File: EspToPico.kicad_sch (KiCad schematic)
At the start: 13 parts, among them J1 Conn_01x20_Pin, J2 Conn_01x20_Pin, J3 USB_C_Receptacle_USB2.0_16P, U2 AP2112K-3.3, U3 TPD3E001DRLR, U4 ESP32-S3-WROOM-1

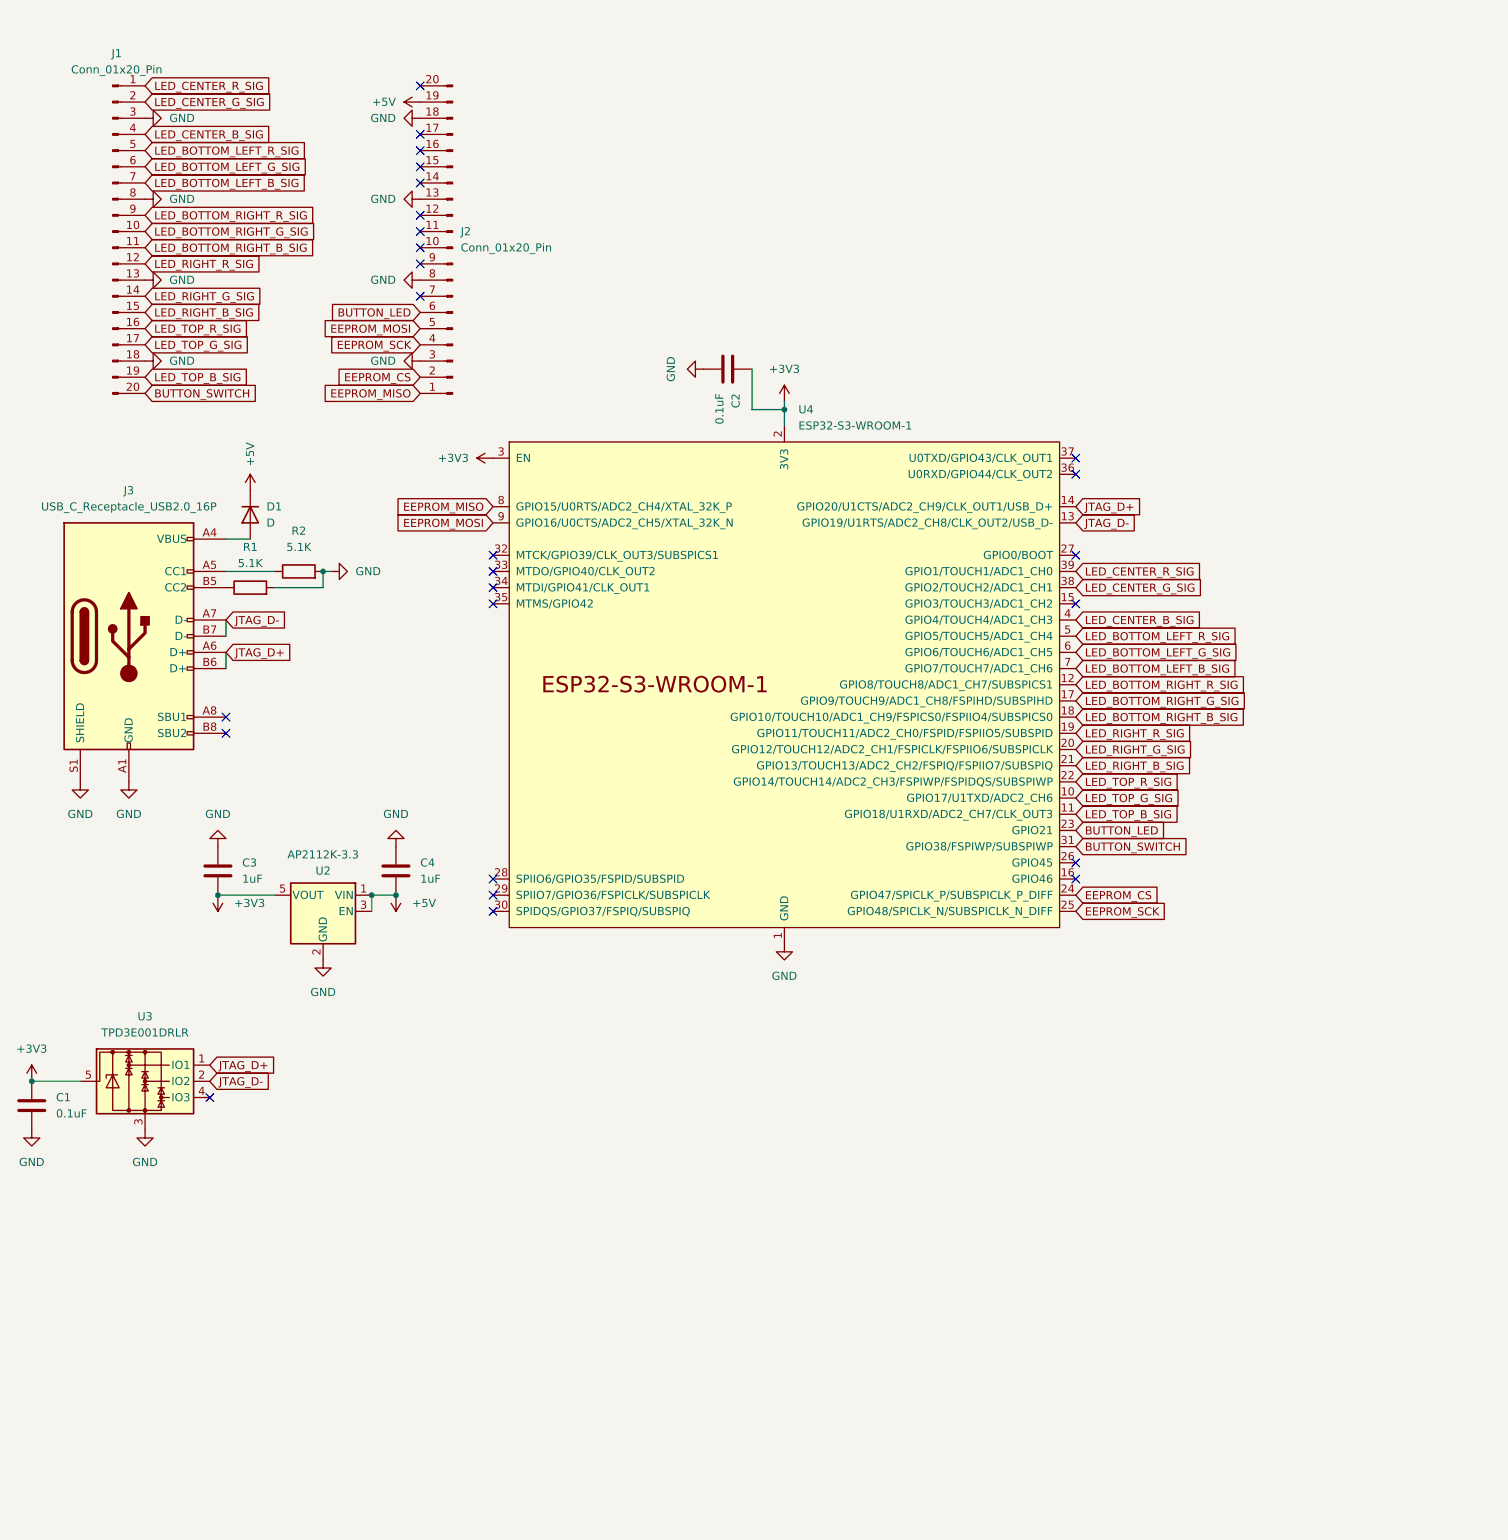
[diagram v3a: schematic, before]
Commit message: Started conversion to ESP32
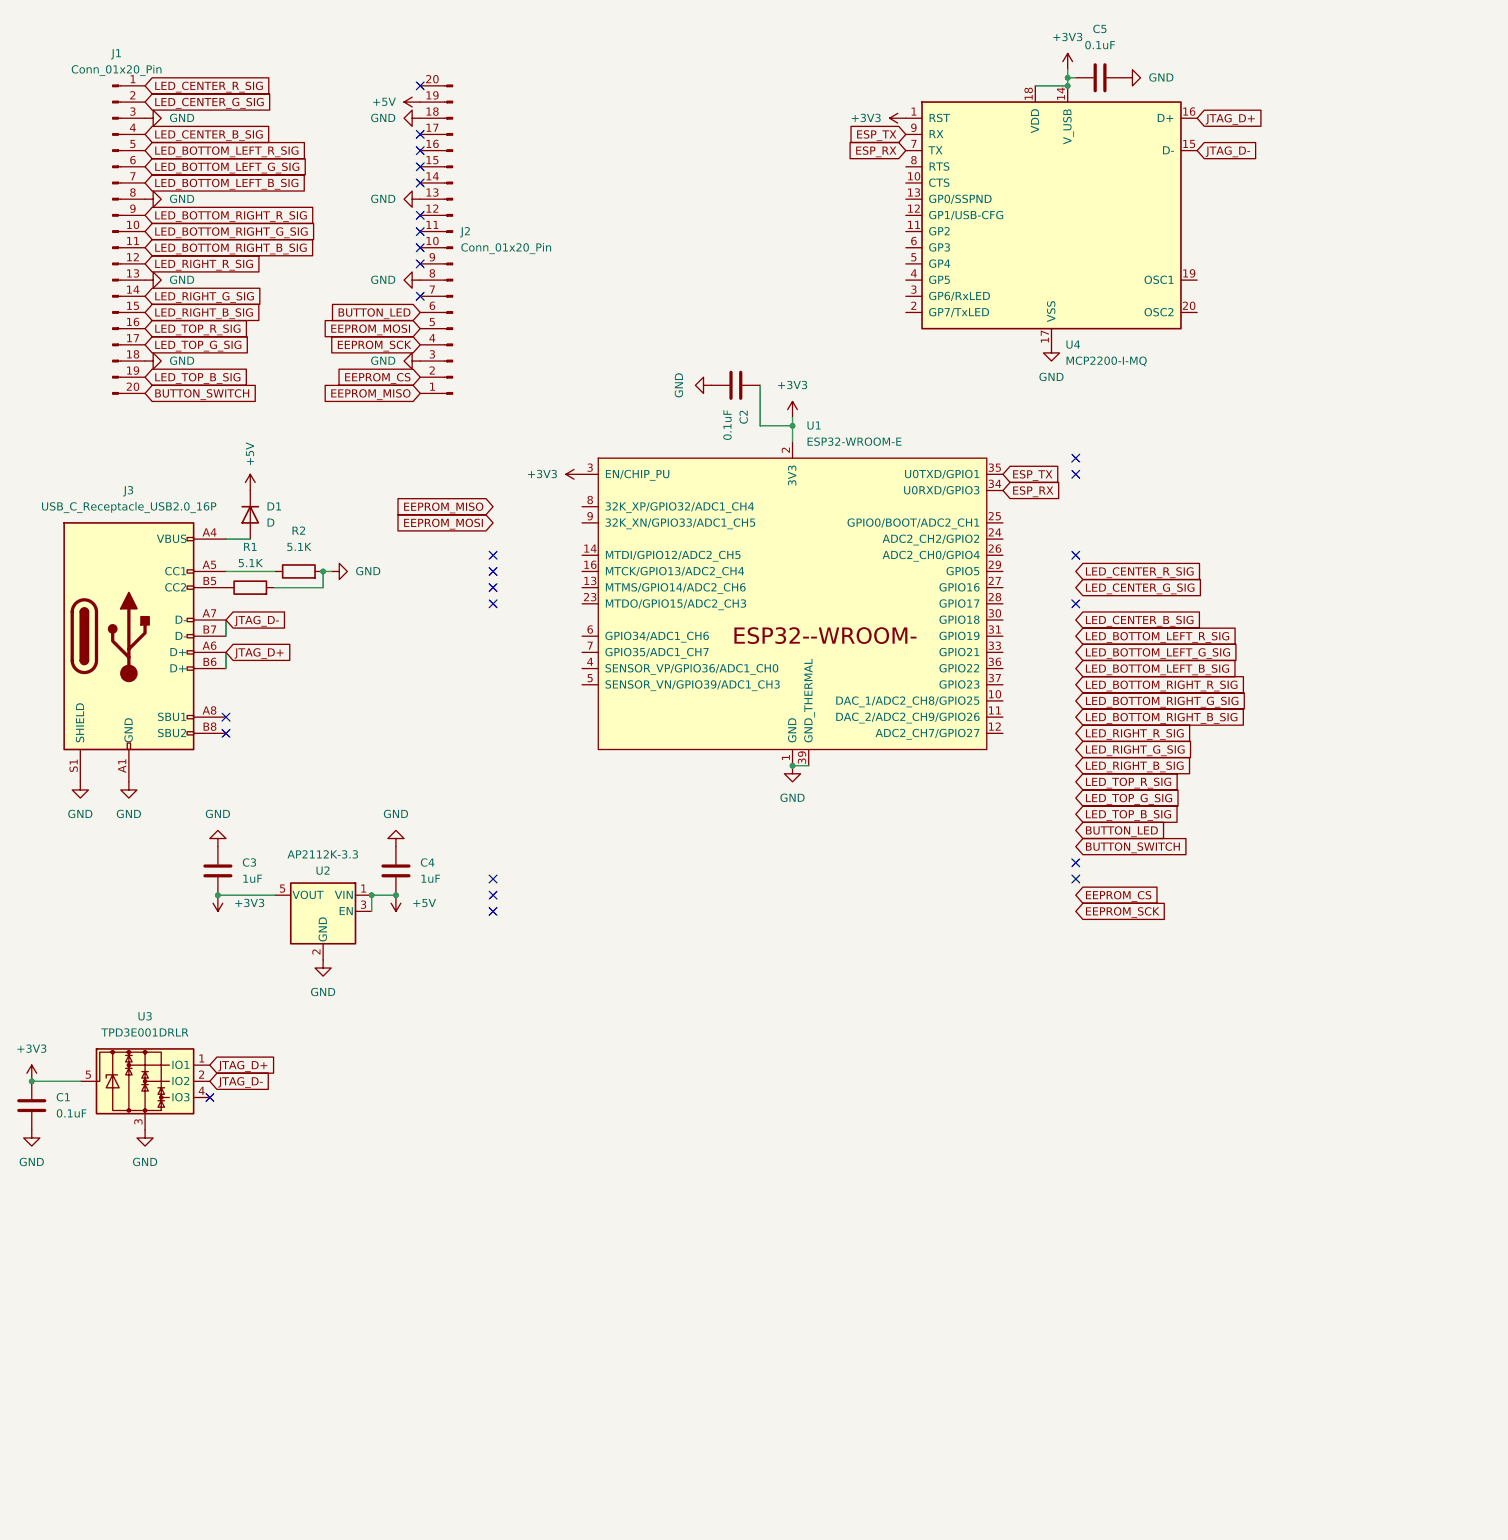
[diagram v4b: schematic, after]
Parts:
- removed U4: ESP32-S3-WROOM-1, PCM_Espressif:ESP32-S3-WROOM-1, symbol PCM_Espressif:ESP32-S3-WROOM-1
- added C5: 0.1uF, symbol Device:C
- added U1: ESP32-WROOM-E, PCM_Espressif:ESP32-WROOM-32E, symbol PCM_Espressif:ESP32-WROOM-E
- added U4: MCP2200-I-MQ, Package_DFN_QFN:QFN-20-1EP_5x5mm_P0.65mm_EP3.35x3.35mm, symbol Interface_USB:MCP2200-I-MQ
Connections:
- net +3V3: now also C5.1, U1.2 (3V3), U1.3 (EN/CHIP_PU), U4.1 (RST), U4.14 (V_USB), U4.18 (VDD)
- net GND: now also C5.2, U1.1 (GND), U1.15 (GND), U1.38 (GND), U1.39 (GND_THERMAL), U4.17 (VSS)
- net JTAG_D+: now also U4.16 (D+)
- net JTAG_D-: now also U4.15 (D-)
- new net ESP_RX: U1.34 (U0RXD/GPIO3), U4.7 (TX)
- new net ESP_TX: U1.35 (U0TXD/GPIO1), U4.9 (RX)
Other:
- moved on the sheet: C2

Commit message: Updated to ESP32
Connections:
- net BUTTON_LED: now also U1.4 (SENSOR_VP/GPIO36/ADC1_CH0)
- net BUTTON_SWITCH: now also U1.23 (MTDO/GPIO15/ADC2_CH3)
- net EEPROM_CS: now also U1.7 (GPIO35/ADC1_CH7)
- net EEPROM_MISO: now also U1.8 (32K_XP/GPIO32/ADC1_CH4)
- net EEPROM_MOSI: now also U1.5 (SENSOR_VN/GPIO39/ADC1_CH3)
- net EEPROM_SCK: now also U1.6 (GPIO34/ADC1_CH6)
- net LED_BOTTOM_LEFT_B_SIG: now also U1.29 (GPIO5)
- net LED_BOTTOM_LEFT_G_SIG: now also U1.30 (GPIO18)
- net LED_BOTTOM_LEFT_R_SIG: now also U1.31 (GPIO19)
- net LED_BOTTOM_RIGHT_B_SIG: now also U1.26 (ADC2_CH0/GPIO4)
- net LED_BOTTOM_RIGHT_G_SIG: now also U1.27 (GPIO16)
- net LED_BOTTOM_RIGHT_R_SIG: now also U1.28 (GPIO17)
- net LED_CENTER_B_SIG: now also U1.33 (GPIO21)
- net LED_CENTER_G_SIG: now also U1.36 (GPIO22)
- net LED_CENTER_R_SIG: now also U1.37 (GPIO23)
- net LED_RIGHT_B_SIG: now also U1.11 (DAC_2/ADC2_CH9/GPIO26)
- net LED_RIGHT_G_SIG: now also U1.10 (DAC_1/ADC2_CH8/GPIO25)
- net LED_RIGHT_R_SIG: now also U1.9 (32K_XN/GPIO33/ADC1_CH5)
- net LED_TOP_B_SIG: now also U1.12 (ADC2_CH7/GPIO27)
- net LED_TOP_G_SIG: now also U1.13 (MTMS/GPIO14/ADC2_CH6)
- net LED_TOP_R_SIG: now also U1.14 (MTDI/GPIO12/ADC2_CH5)
- no-connect marks 26 -> 28

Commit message: Electrical and Routing fixes
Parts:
- added Y1: CSTNE12M0GH5L000R0, footprints:CSTCE12M0G15L, symbol Device:Resonator
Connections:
- net GND: now also Y1.2
- net at U4.19 (OSC1): now also Y1.3
- net at U4.20 (OSC2): now also Y1.1
- no-connect marks 28 -> 26
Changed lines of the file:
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@@
 	)
 	(no_connect
-		(at 231.14 54.61)
-	)
-	(no_connect
 		(at 185.42 46.99)
 	)
@@
 		(at 185.42 54.61)
 	)
-	(no_connect
-		(at 231.14 59.69)
+	(wire
+		(pts
+			(xy 237.49 60.96) (xy 259.08 60.96)
+		)
+		(stroke
+			(width 0)
+			(type default)
+		)
 	)
 	(wire
@@
 	(wire
 		(pts
+			(xy 237.49 59.69) (xy 237.49 60.96)
+		)
+		(stroke
+			(width 0)
+			(type default)
+		)
+	)
+	(wire
+		(pts
 			(xy 78.74 110.49) (xy 78.74 107.95)
 		)
@@
 	(wire
 		(pts
+			(xy 231.14 54.61) (xy 237.49 54.61)
+		)
+		(stroke
+			(width 0)
+			(type default)
+		)
+	)
+	(wire
+		(pts
+			(xy 237.49 53.34) (xy 259.08 53.34)
+		)
+		(stroke
+			(width 0)
+			(type default)
+		)
+	)
+	(wire
+		(pts
 			(xy 86.36 100.33) (xy 78.74 100.33)
 		)
@@
 	(wire
 		(pts
+			(xy 231.14 59.69) (xy 237.49 59.69)
+		)
+		(stroke
+			(width 0)
+			(type default)
+		)
+	)
+	(wire
+		(pts
 			(xy 93.98 102.87) (xy 93.98 100.33)
 		)
@@
 	(wire
 		(pts
+			(xy 237.49 54.61) (xy 237.49 53.34)
+		)
+		(stroke
+			(width 0)
+			(type default)
+		)
+	)
+	(wire
+		(pts
 			(xy 205.74 24.13) (xy 210.82 24.13)
 		)
@@
 	)
 	(symbol
+		(lib_id "power:GND")
+		(at 264.16 57.15 90)
+		(unit 1)
+		(exclude_from_sim no)
+		(in_bom yes)
+		(on_board yes)
+		(dnp no)
+		(fields_autoplaced yes)
+		(property "Reference" "#PWR030"
+			(at 270.51 57.15 0)
+			(effects
+				(font
+					(size 1.27 1.27)
+				)
+				(hide yes)
+			)
+		)
+		(property "Value" "GND"
+			(at 267.97 57.1499 90)
+			(effects
+				(font
+					(size 1.27 1.27)
+				)
+				(justify right)
+			)
+		)
+		(property "Footprint" ""
+			(at 264.16 57.15 0)
+			(effects
+				(font
+					(size 1.27 1.27)
+				)
+				(hide yes)
+			)
+		)
+		(property "Datasheet" ""
+			(at 264.16 57.15 0)
+			(effects
+				(font
+					(size 1.27 1.27)
+				)
+				(hide yes)
+			)
+		)
+		(property "Description" "Power symbol creates a global label with name \"GND\" , ground"
+			(at 264.16 57.15 0)
+			(effects
+				(font
+					(size 1.27 1.27)
+				)
+				(hide yes)
+			)
+		)
+		(pin "1"
+		)
+		(instances
+			(project "EspToPico"
+				(path "/7a8b5c67-f9f8-419b-9ddd-ea239e074577"
+					(reference "#PWR030")
+					(unit 1)
+				)
+			)
+		)
+	)
+	(symbol
 		(lib_id "power:+3V3")
 		(at 185.42 29.21 90)
@@
 					(unit 1)
 				)
+			)
+		)
+	)
+	(symbol
+		(lib_id "Device:Resonator")
+		(at 259.08 57.15 90)
+		(unit 1)
+		(exclude_from_sim no)
+		(in_bom yes)
+		(on_board yes)
+		(dnp no)
+		(fields_autoplaced yes)
+		(property "Reference" "Y1"
+			(at 255.27 55.8799 90)
+			(effects
+				(font
+					(size 1.27 1.27)
+				)
+				(justify left)
+			)
+		)
+		(property "Value" "CSTNE12M0GH5L000R0"
+			(at 255.27 58.4199 90)
+			(effects
+				(font
+					(size 1.27 1.27)
+				)
+				(justify left)
+			)
+		)
+		(property "Footprint" "footprints:CSTCE12M0G15L"
+			(at 259.08 57.785 0)
+			(effects
+				(font
+					(size 1.27 1.27)
+				)
+				(hide yes)
+			)
+		)
+		(property "Datasheet" "~"
+			(at 259.08 57.785 0)
+			(effects
+				(font
+					(size 1.27 1.27)
+				)
+				(hide yes)
+			)
+		)
+		(property "Description" "Three pin ceramic resonator"
+			(at 259.08 57.15 0)
+			(effects
+				(font
+					(size 1.27 1.27)
+				)
+				(hide yes)
+			)
+		)
+		(pin "1"
+		)
+		(pin "2"
+		)
+		(pin "3"
+		)
+		(instances
+			(project ""
+				(path "/7a8b5c67-f9f8-419b-9ddd-ea239e074577"
+					(reference "Y1")
+					(unit 1)
+				)
